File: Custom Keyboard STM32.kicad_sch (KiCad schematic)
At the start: 315 parts

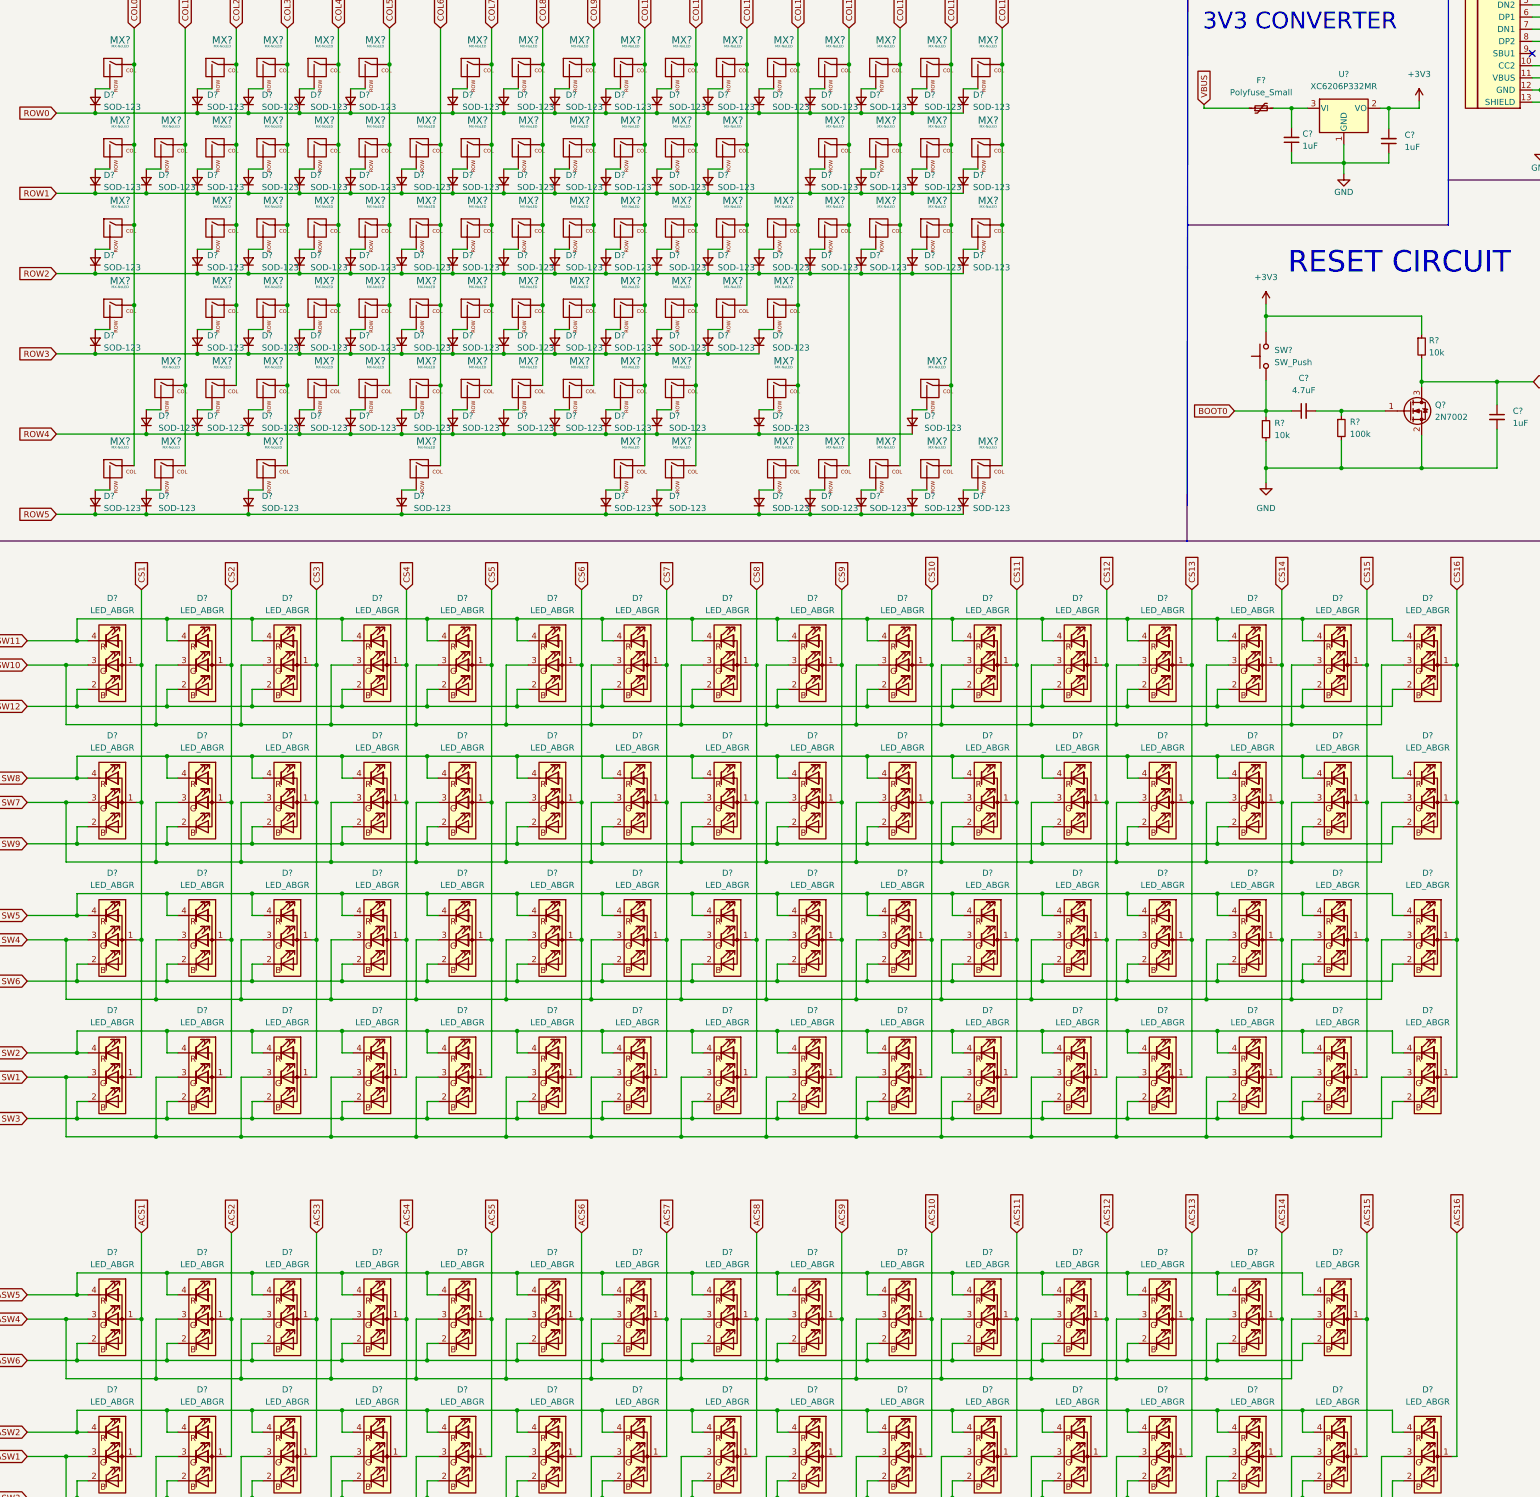
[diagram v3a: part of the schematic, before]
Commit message: D? --> LED?
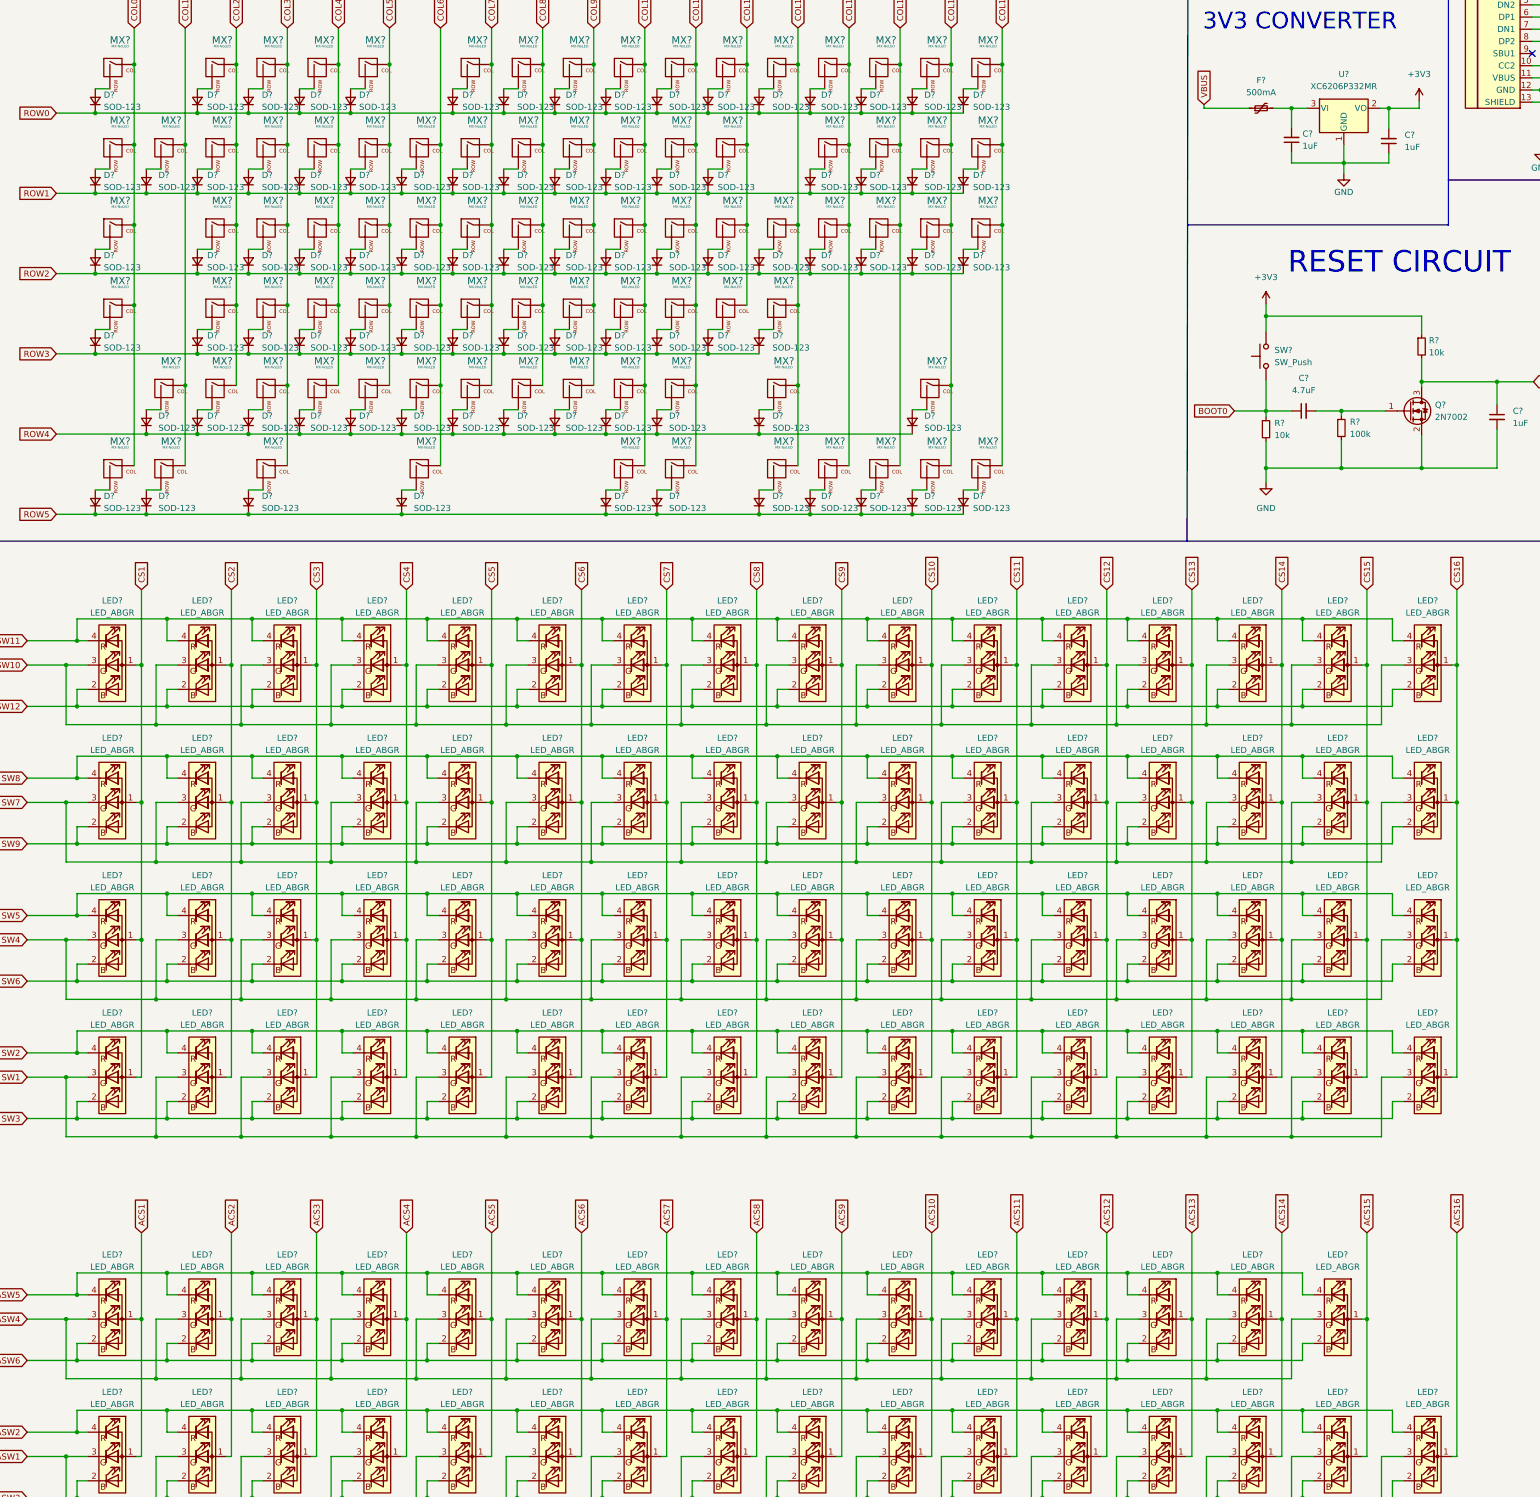
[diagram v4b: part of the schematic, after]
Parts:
- removed D? (x95): LED_ABGR, symbol BgrA:LED_ABGR
- added LED? (x95): LED_ABGR, symbol BgrA:LED_ABGR
- F?: value Polyfuse_Small -> 500mA
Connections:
- net ACS1: now also LED?.1 (A), LED?.1 (A)
- net ACS10: now also LED?.1 (A), LED?.1 (A)
- net ACS11: now also LED?.1 (A), LED?.1 (A)
- net ACS12: now also LED?.1 (A), LED?.1 (A)
- net ACS13: now also LED?.1 (A), LED?.1 (A)
- net ACS14: now also LED?.1 (A), LED?.1 (A)
- net ACS15: now also LED?.1 (A), LED?.1 (A)
- net ACS16: now also LED?.1 (A)
- net ACS2: now also LED?.1 (A), LED?.1 (A)
- net ACS3: now also LED?.1 (A), LED?.1 (A)
- net ACS4: now also LED?.1 (A), LED?.1 (A)
- net ACS5: now also LED?.1 (A), LED?.1 (A)
- net ACS6: now also LED?.1 (A), LED?.1 (A)
- net ACS7: now also LED?.1 (A), LED?.1 (A)
- net ACS8: now also LED?.1 (A), LED?.1 (A)
- net ACS9: now also LED?.1 (A), LED?.1 (A)
- net ASW1: now also LED?.3 (GK), LED?.3 (GK), LED?.3 (GK), LED?.3 (GK), LED?.3 (GK), LED?.3 (GK), LED?.3 (GK), LED?.3 (GK), LED?.3 (GK), LED?.3 (GK), LED?.3 (GK), LED?.3 (GK), LED?.3 (GK), LED?.3 (GK), LED?.3 (GK), LED?.3 (GK)
- net ASW2: now also LED?.4 (RK), LED?.4 (RK), LED?.4 (RK), LED?.4 (RK), LED?.4 (RK), LED?.4 (RK), LED?.4 (RK), LED?.4 (RK), LED?.4 (RK), LED?.4 (RK), LED?.4 (RK), LED?.4 (RK), LED?.4 (RK), LED?.4 (RK), LED?.4 (RK), LED?.4 (RK)
- net ASW3: now also LED?.2 (BK), LED?.2 (BK), LED?.2 (BK), LED?.2 (BK), LED?.2 (BK), LED?.2 (BK), LED?.2 (BK), LED?.2 (BK), LED?.2 (BK), LED?.2 (BK), LED?.2 (BK), LED?.2 (BK), LED?.2 (BK), LED?.2 (BK), LED?.2 (BK), LED?.2 (BK)
- net ASW4: now also LED?.3 (GK), LED?.3 (GK), LED?.3 (GK), LED?.3 (GK), LED?.3 (GK), LED?.3 (GK), LED?.3 (GK), LED?.3 (GK), LED?.3 (GK), LED?.3 (GK), LED?.3 (GK), LED?.3 (GK), LED?.3 (GK), LED?.3 (GK), LED?.3 (GK)
- net ASW5: now also LED?.4 (RK), LED?.4 (RK), LED?.4 (RK), LED?.4 (RK), LED?.4 (RK), LED?.4 (RK), LED?.4 (RK), LED?.4 (RK), LED?.4 (RK), LED?.4 (RK), LED?.4 (RK), LED?.4 (RK), LED?.4 (RK), LED?.4 (RK), LED?.4 (RK)
- net ASW6: now also LED?.2 (BK), LED?.2 (BK), LED?.2 (BK), LED?.2 (BK), LED?.2 (BK), LED?.2 (BK), LED?.2 (BK), LED?.2 (BK), LED?.2 (BK), LED?.2 (BK), LED?.2 (BK), LED?.2 (BK), LED?.2 (BK), LED?.2 (BK), LED?.2 (BK)
- net CS1: now also LED?.1 (A), LED?.1 (A), LED?.1 (A), LED?.1 (A)
- net CS10: now also LED?.1 (A), LED?.1 (A), LED?.1 (A), LED?.1 (A)
- net CS11: now also LED?.1 (A), LED?.1 (A), LED?.1 (A), LED?.1 (A)
- net CS12: now also LED?.1 (A), LED?.1 (A), LED?.1 (A), LED?.1 (A)
- net CS13: now also LED?.1 (A), LED?.1 (A), LED?.1 (A), LED?.1 (A)
- net CS14: now also LED?.1 (A), LED?.1 (A), LED?.1 (A), LED?.1 (A)
- net CS15: now also LED?.1 (A), LED?.1 (A), LED?.1 (A), LED?.1 (A)
- net CS16: now also LED?.1 (A), LED?.1 (A), LED?.1 (A), LED?.1 (A)
- net CS2: now also LED?.1 (A), LED?.1 (A), LED?.1 (A), LED?.1 (A)
- net CS3: now also LED?.1 (A), LED?.1 (A), LED?.1 (A), LED?.1 (A)
- net CS4: now also LED?.1 (A), LED?.1 (A), LED?.1 (A), LED?.1 (A)
- net CS5: now also LED?.1 (A), LED?.1 (A), LED?.1 (A), LED?.1 (A)
- net CS6: now also LED?.1 (A), LED?.1 (A), LED?.1 (A), LED?.1 (A)
- net CS7: now also LED?.1 (A), LED?.1 (A), LED?.1 (A), LED?.1 (A)
- net CS8: now also LED?.1 (A), LED?.1 (A), LED?.1 (A), LED?.1 (A)
- net CS9: now also LED?.1 (A), LED?.1 (A), LED?.1 (A), LED?.1 (A)
- net SW1: now also LED?.3 (GK), LED?.3 (GK), LED?.3 (GK), LED?.3 (GK), LED?.3 (GK), LED?.3 (GK), LED?.3 (GK), LED?.3 (GK), LED?.3 (GK), LED?.3 (GK), LED?.3 (GK), LED?.3 (GK), LED?.3 (GK), LED?.3 (GK), LED?.3 (GK), LED?.3 (GK)
- net SW10: now also LED?.3 (GK), LED?.3 (GK), LED?.3 (GK), LED?.3 (GK), LED?.3 (GK), LED?.3 (GK), LED?.3 (GK), LED?.3 (GK), LED?.3 (GK), LED?.3 (GK), LED?.3 (GK), LED?.3 (GK), LED?.3 (GK), LED?.3 (GK), LED?.3 (GK), LED?.3 (GK)
- net SW11: now also LED?.4 (RK), LED?.4 (RK), LED?.4 (RK), LED?.4 (RK), LED?.4 (RK), LED?.4 (RK), LED?.4 (RK), LED?.4 (RK), LED?.4 (RK), LED?.4 (RK), LED?.4 (RK), LED?.4 (RK), LED?.4 (RK), LED?.4 (RK), LED?.4 (RK), LED?.4 (RK)
- net SW12: now also LED?.2 (BK), LED?.2 (BK), LED?.2 (BK), LED?.2 (BK), LED?.2 (BK), LED?.2 (BK), LED?.2 (BK), LED?.2 (BK), LED?.2 (BK), LED?.2 (BK), LED?.2 (BK), LED?.2 (BK), LED?.2 (BK), LED?.2 (BK), LED?.2 (BK), LED?.2 (BK)
- net SW2: now also LED?.4 (RK), LED?.4 (RK), LED?.4 (RK), LED?.4 (RK), LED?.4 (RK), LED?.4 (RK), LED?.4 (RK), LED?.4 (RK), LED?.4 (RK), LED?.4 (RK), LED?.4 (RK), LED?.4 (RK), LED?.4 (RK), LED?.4 (RK), LED?.4 (RK), LED?.4 (RK)
- net SW3: now also LED?.2 (BK), LED?.2 (BK), LED?.2 (BK), LED?.2 (BK), LED?.2 (BK), LED?.2 (BK), LED?.2 (BK), LED?.2 (BK), LED?.2 (BK), LED?.2 (BK), LED?.2 (BK), LED?.2 (BK), LED?.2 (BK), LED?.2 (BK), LED?.2 (BK), LED?.2 (BK)
- net SW4: now also LED?.3 (GK), LED?.3 (GK), LED?.3 (GK), LED?.3 (GK), LED?.3 (GK), LED?.3 (GK), LED?.3 (GK), LED?.3 (GK), LED?.3 (GK), LED?.3 (GK), LED?.3 (GK), LED?.3 (GK), LED?.3 (GK), LED?.3 (GK), LED?.3 (GK), LED?.3 (GK)
- net SW5: now also LED?.4 (RK), LED?.4 (RK), LED?.4 (RK), LED?.4 (RK), LED?.4 (RK), LED?.4 (RK), LED?.4 (RK), LED?.4 (RK), LED?.4 (RK), LED?.4 (RK), LED?.4 (RK), LED?.4 (RK), LED?.4 (RK), LED?.4 (RK), LED?.4 (RK), LED?.4 (RK)
- net SW6: now also LED?.2 (BK), LED?.2 (BK), LED?.2 (BK), LED?.2 (BK), LED?.2 (BK), LED?.2 (BK), LED?.2 (BK), LED?.2 (BK), LED?.2 (BK), LED?.2 (BK), LED?.2 (BK), LED?.2 (BK), LED?.2 (BK), LED?.2 (BK), LED?.2 (BK), LED?.2 (BK)
- net SW7: now also LED?.3 (GK), LED?.3 (GK), LED?.3 (GK), LED?.3 (GK), LED?.3 (GK), LED?.3 (GK), LED?.3 (GK), LED?.3 (GK), LED?.3 (GK), LED?.3 (GK), LED?.3 (GK), LED?.3 (GK), LED?.3 (GK), LED?.3 (GK), LED?.3 (GK), LED?.3 (GK)
- net SW8: now also LED?.4 (RK), LED?.4 (RK), LED?.4 (RK), LED?.4 (RK), LED?.4 (RK), LED?.4 (RK), LED?.4 (RK), LED?.4 (RK), LED?.4 (RK), LED?.4 (RK), LED?.4 (RK), LED?.4 (RK), LED?.4 (RK), LED?.4 (RK), LED?.4 (RK), LED?.4 (RK)
- net SW9: now also LED?.2 (BK), LED?.2 (BK), LED?.2 (BK), LED?.2 (BK), LED?.2 (BK), LED?.2 (BK), LED?.2 (BK), LED?.2 (BK), LED?.2 (BK), LED?.2 (BK), LED?.2 (BK), LED?.2 (BK), LED?.2 (BK), LED?.2 (BK), LED?.2 (BK), LED?.2 (BK)

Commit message: 1
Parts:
- added U?: SRV05-4, Package_TO_SOT_SMD:SOT-23-6, symbol Power_Protection:SRV05-4
- R5, R6: renamed from R?; value 20k -> 30k
- gave numbers to parts that had none: 313
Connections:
- net GND: now also U?.2 (VN)
- net VBUS: now also U?.5 (VP)
- net DN renamed D-
- net D-: now also U?.6 (IO4)
- net DP renamed D+
- net D+: now also U?.1 (IO1)
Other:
- note added: "ESD"
- note added: "THT R"

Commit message: 1
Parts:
- removed U?: SRV05-4, Package_TO_SOT_SMD:SOT-23-6, symbol Power_Protection:SRV05-4
- added F2: 750mA, symbol Device:Polyfuse_Small
- added U5: SRV05-4, marbastlib-various:SOT-23-6-routable, symbol marbastlib-various:SRV05-4
- C1, C10, C11, C12, C13, C14, C15, C16, C17, C18, C19, C2, C20, C21, C22, C23, C24, C25, C26, C3, C4, C5, C6, C7, C8, C9: footprint (none) -> Capacitor_SMD:C_0805_2012Metric
- D1, D10, D11, D12, D13, D14, D15, D16, D17, D18, D19, D2, D20, D21, D22, D23, D24, D25, D26, D27, D28, D29, D3, D30, D31, D32, D33, D34, D35, D36, D37, D38, D39, D4, D40, D41, D42, D43, D44, D45, D46, D47, D48, D49, D5, D50, D51, D52, D53, D54, D55, D56, D57, D58, D59, D6, D60, D61, D62, D63, D64, D65, D66, D67, D68, D69, D7, D70, D71, D72, D73, D74, D75, D76, D77, D78, D79, D8, D80, D81, D82, D83, D84, D85, D86, D87, D9: footprint (none) -> Diode_SMD:D_SOD-123
- MX1, MX10, MX11, MX12, MX13, MX14, MX15, MX16, MX17, MX18, MX19, MX2, MX20, MX21, MX22, MX23, MX24, MX25, MX26, MX27, MX28, MX29, MX3, MX31, MX32, MX33, MX35, MX36, MX37, MX38, MX39, MX4, MX40, MX41, MX42, MX43, MX44, MX45, MX46, MX48, MX49, MX5, MX50, MX52, MX53, MX54, MX55, MX56, MX57, MX58, MX59, MX6, MX60, MX61, MX62, MX65, MX66, MX67, MX68, MX69, MX7, MX70, MX71, MX72, MX73, MX74, MX76, MX8, MX85, MX86, MX87, MX9: footprint (none) -> marbastlib-mx:SW_MX_HS_1u
- MX30: footprint (none) -> marbastlib-mx:STAB_MX_P_2u
- MX34, MX47: footprint (none) -> marbastlib-mx:SW_MX_HS_1.5u
- MX51: footprint (none) -> marbastlib-mx:SW_MX_HS_1.75u
- MX63, MX64: footprint (none) -> marbastlib-mx:STAB_MX_P_2.25u
- MX75: footprint (none) -> marbastlib-mx:STAB_MX_P_2.75u
- MX77, MX78, MX79, MX81, MX82, MX83, MX84: footprint (none) -> marbastlib-mx:SW_MX_HS_1.25u
- MX80: footprint (none) -> marbastlib-mx:STAB_MX_P_6.25u
- R1, R10, R11, R2, R3, R4, R6, R7, R8, R9: footprint (none) -> Resistor_SMD:R_0805_2012Metric
- USB1: footprint (none) -> marbastlib-various:USB_C_Receptacle_HRO_TYPE-C-31-M-14
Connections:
- net D+: now also U5.1 (IO1)
- net D-: now also U5.4 (IO3)
- net GND: now also U5.2 (VN)
- net VBUS: now also F2.1
- new net: F2.2, U5.5 (VP)
